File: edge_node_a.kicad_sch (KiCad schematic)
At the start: 5 parts

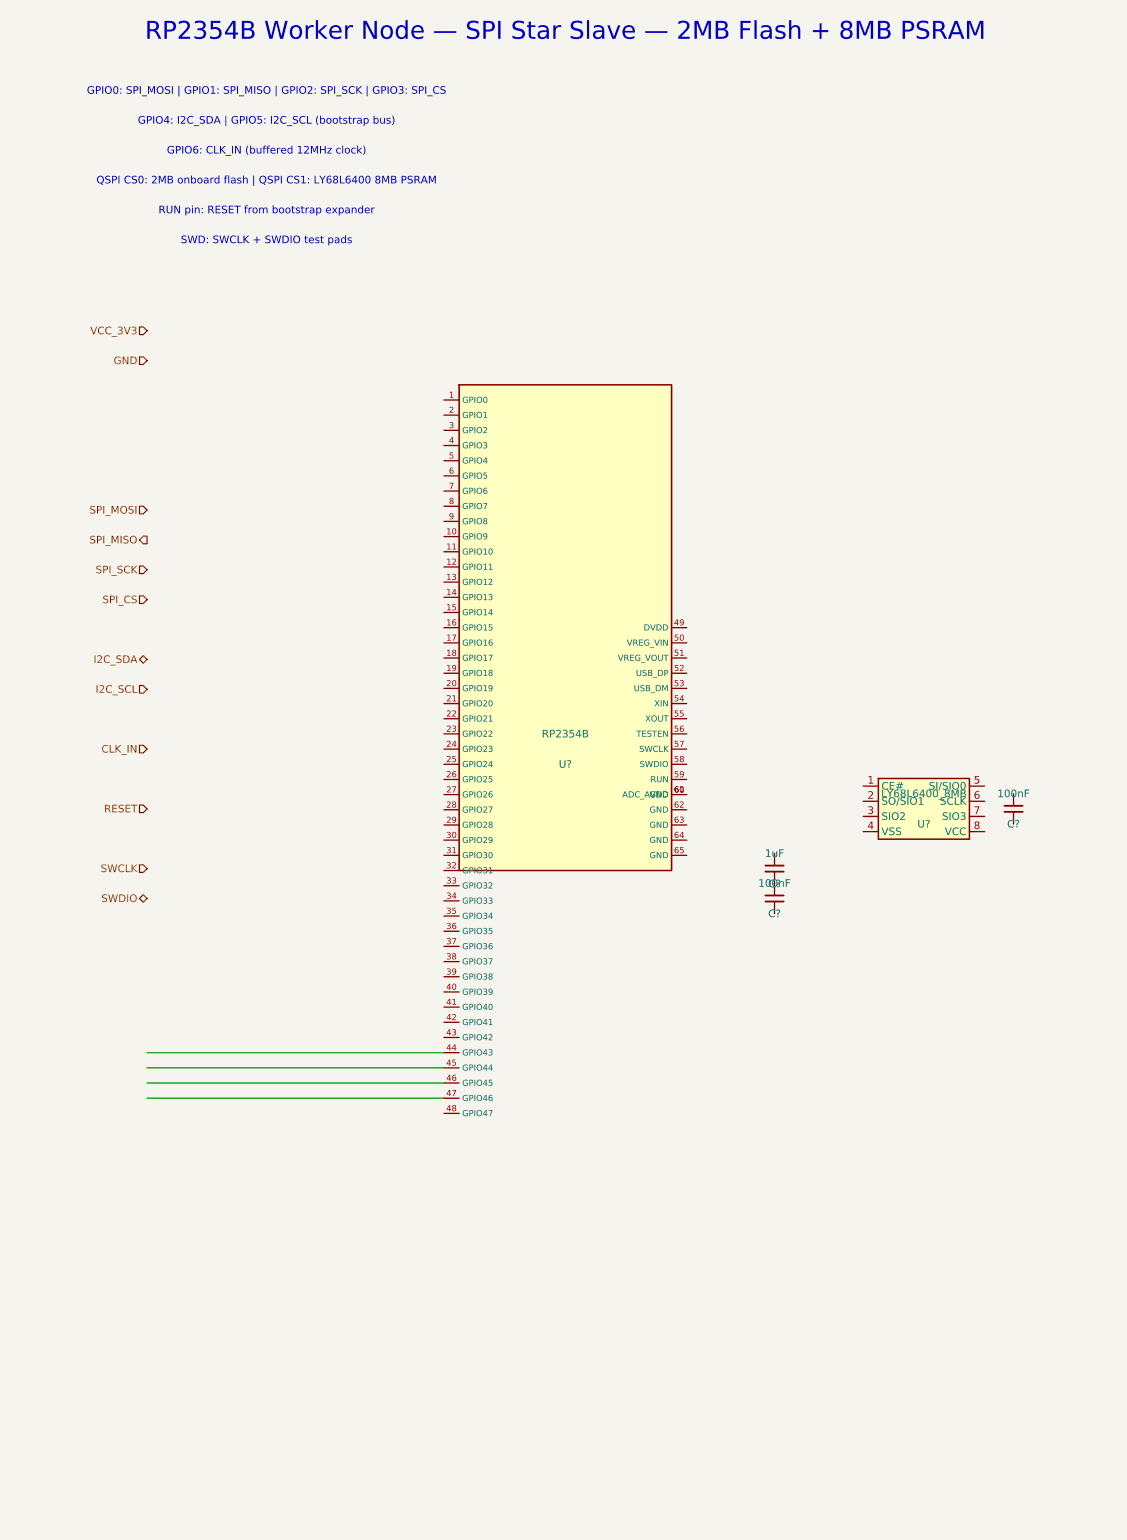
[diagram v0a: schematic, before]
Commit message: Regenerate KiCad output files for v1.0 architecture
Co-authored-by: Copilot <223556219+Copilot@users.noreply.github.com>
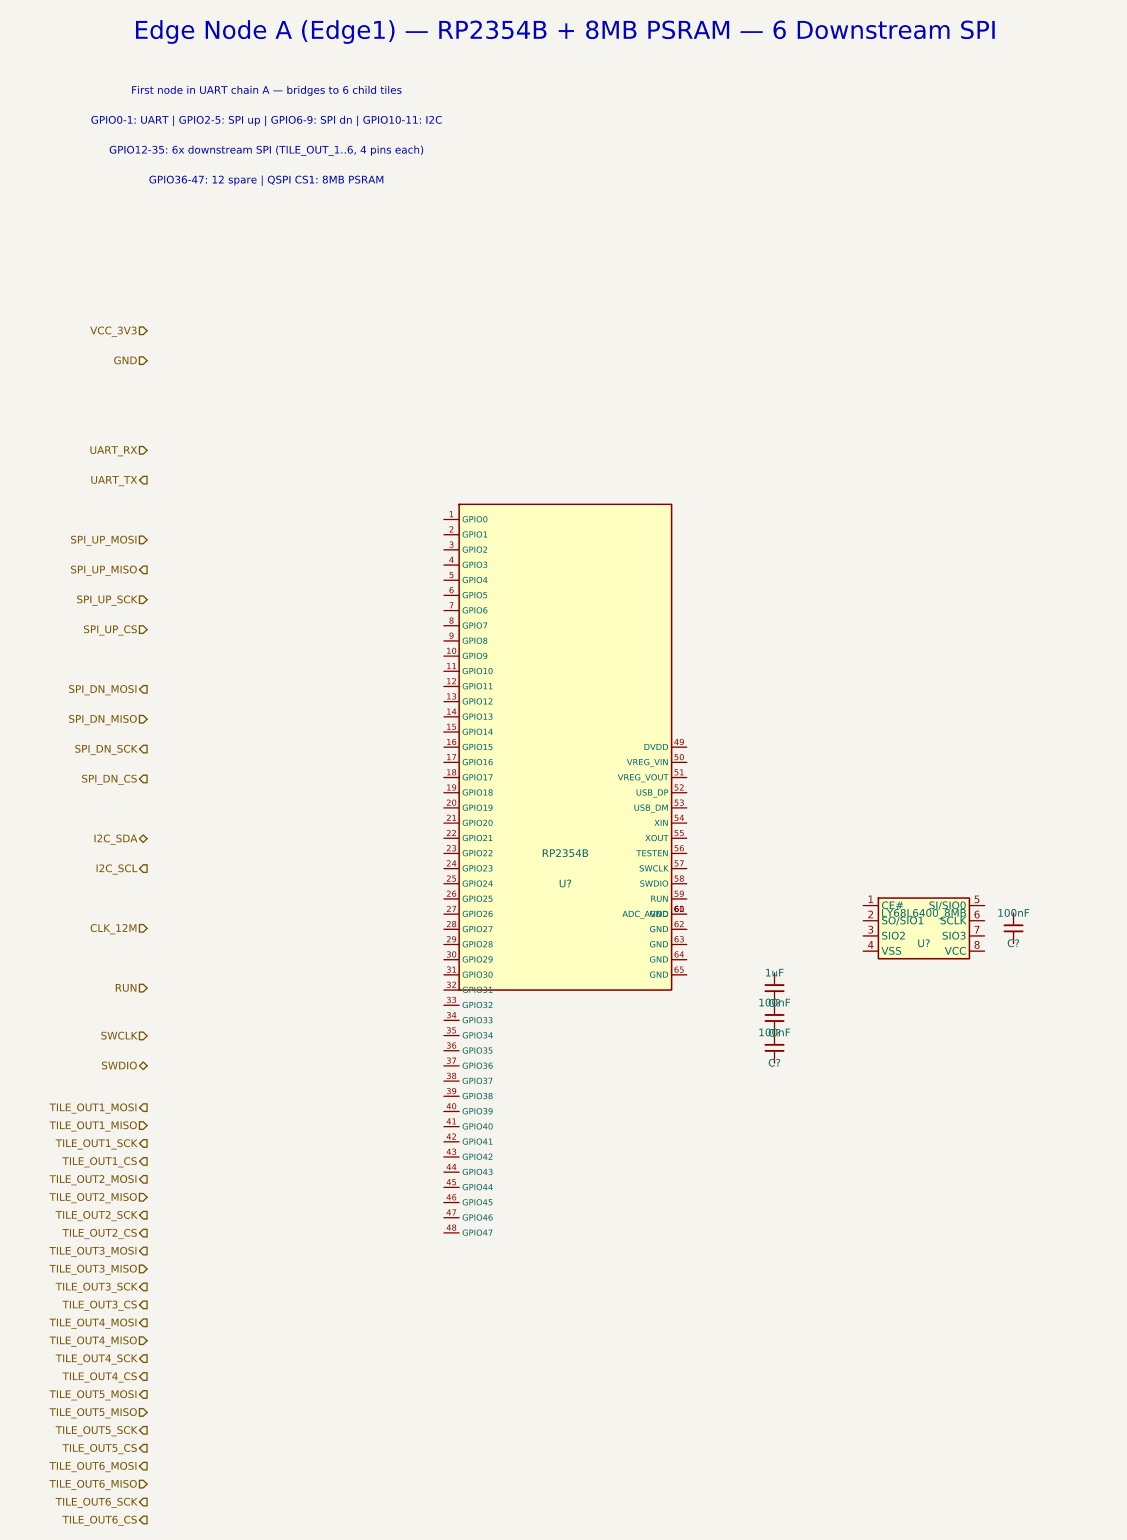
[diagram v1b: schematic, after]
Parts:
- removed C? (x2): 100nF, symbol Device:C
- removed C?: 1uF, symbol Device:C
- removed U?: RP2354B, symbol MCU_RaspberryPi:RP2354B
- removed U?: LY68L6400_8MB, symbol Memory_RAM:LY68L6400
- added C? (x3): 100nF, symbol Device:C
- added C?: 1uF, symbol Device:C
- added U?: RP2354B, symbol MCU_RaspberryPi:RP2354B
- added U?: LY68L6400_8MB, symbol Memory_RAM:LY68L6400
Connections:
- new net: U?.60 (ADC_AVDD), U?.61 (GND)
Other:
- note added: "Edge Node A (Edge1) — RP2354B + 8MB PSRAM — 6 Downstream SPI"
- note added: "First node in UART chain A — bridges to 6 child tiles"
- note added: "GPIO0-1: UART | GPIO2-5: SPI up | GPIO6-9: SPI dn | GPIO10-11: I2C"
- note added: "GPIO12-35: 6x downstream SPI (TILE_OUT_1..6, 4 pins each)"
- note added: "GPIO36-47: 12 spare | QSPI CS1: 8MB PSRAM"
- note removed: "GPIO0: SPI_MOSI | GPIO1: SPI_MISO | GPIO2: SPI_SCK | GPIO3: SPI_CS"
- note removed: "GPIO4: I2C_SDA | GPIO5: I2C_SCL (bootstrap bus)"
- note removed: "GPIO6: CLK_IN (buffered 12MHz clock)"
- note removed: "QSPI CS0: 2MB onboard flash | QSPI CS1: LY68L6400 8MB PSRAM"
- note removed: "RP2354B Worker Node — SPI Star Slave — 2MB Flash + 8MB PSRAM"
- note removed: "RUN pin: RESET from bootstrap expander"
- note removed: "SWD: SWCLK + SWDIO test pads"
- title: Worker Node (RP2354B + 8MB PSRAM) — SPI Star Slave -> Edge Node A (Edge1) — 6 Downstream SPI + PSRAM
